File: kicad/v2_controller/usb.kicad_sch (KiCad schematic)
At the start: 23 parts, among them J1 USB_C_Receptacle_USB2.0, J2 USB_C_Receptacle_USB2.0, U4 NCP167BMX330TBG, U5 USBLC6-2P6, U6 USBLC6-2P6, U7 CP2102N-Axx-xQFN24

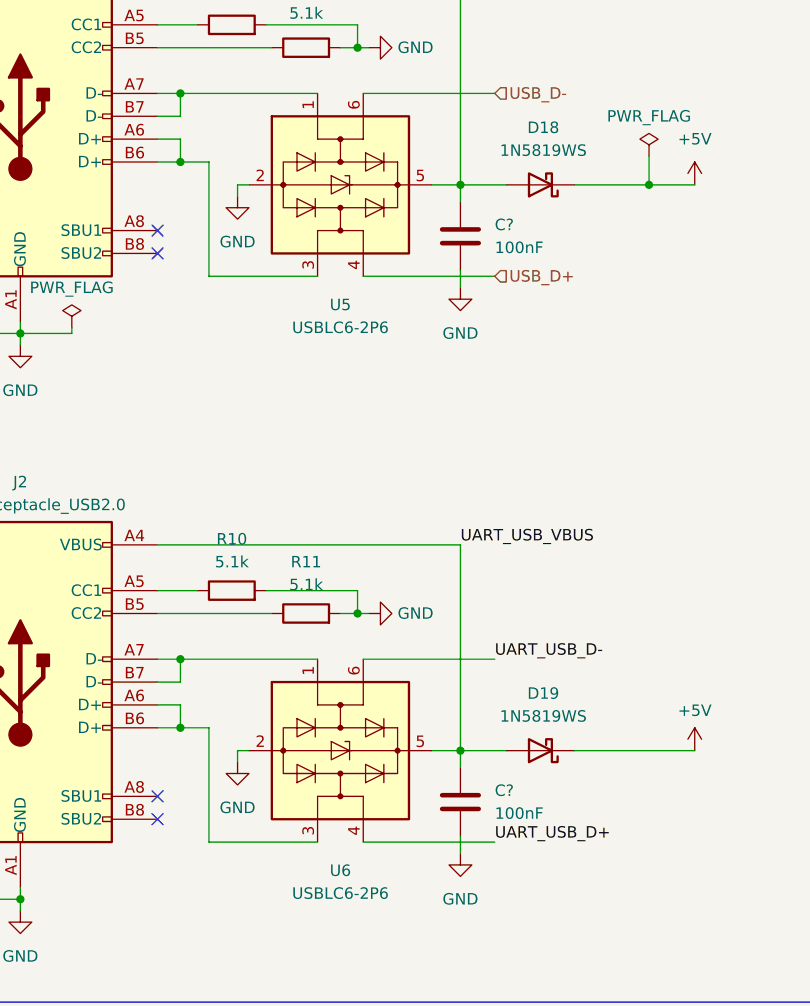
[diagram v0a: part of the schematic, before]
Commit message: [kicad] begin routing some traces
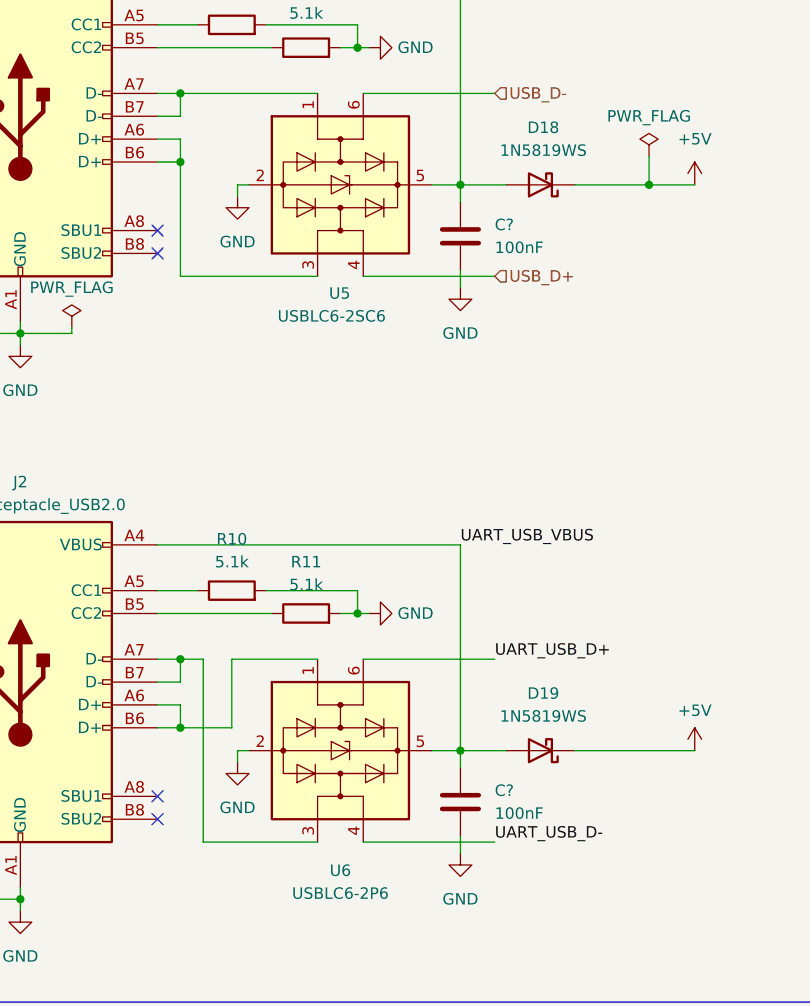
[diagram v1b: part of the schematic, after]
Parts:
- U5: value USBLC6-2P6 -> USBLC6-2SC6; footprint Package_TO_SOT_SMD:SOT-666 -> Package_TO_SOT_SMD:SOT-23-6; symbol Power_Protection:USBLC6-2P6 -> Power_Protection:USBLC6-2SC6; LCSC Part # C2827693 -> C2827654
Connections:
- net UART_USB_D+: now also U6.6 (I/O1); no longer U6.4 (I/O2)
- net UART_USB_D-: now also U6.4 (I/O2); no longer U6.6 (I/O1)
- net at J2.A7 (D-), J2.B7 (D-): now also U6.3 (I/O2); no longer U6.1 (I/O1)
- net at J2.A6 (D+), J2.B6 (D+): now also U6.1 (I/O1); no longer U6.3 (I/O2)
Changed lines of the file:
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@@
   (junction (at 175.895 69.215) (diameter 0) (color 0 0 0 0)
   )
+  (junction (at 63.5 54.61) (diameter 0) (color 0 0 0 0)
+  )
   (junction (at 213.36 42.545) (diameter 0) (color 0 0 0 0)
   )
+  (junction (at 63.5 109.855) (diameter 0) (color 0 0 0 0)
+  )
+  (junction (at 45.72 73.66) (diameter 0) (color 0 0 0 0)
+  )
+  (junction (at 213.36 34.925) (diameter 0) (color 0 0 0 0)
+  )
+  (junction (at 91.44 177.8) (diameter 0) (color 0 0 0 0)
+  )
+  (junction (at 91.44 175.26) (diameter 0) (color 0 0 0 0)
+  )
+  (junction (at 94.615 120.015) (diameter 0) (color 0 0 0 0)
+  )
+  (junction (at 45.72 136.525) (diameter 0) (color 0 0 0 0)
+  )
+  (junction (at 213.36 45.72) (diameter 0) (color 0 0 0 0)
+  )
+  (junction (at 95.25 167.64) (diameter 0) (color 0 0 0 0)
+  )
   (junction (at 63.5 46.99) (diameter 0) (color 0 0 0 0)
   )
-  (junction (at 45.72 73.66) (diameter 0) (color 0 0 0 0)
-  )
-  (junction (at 213.36 34.925) (diameter 0) (color 0 0 0 0)
-  )
-  (junction (at 91.44 177.8) (diameter 0) (color 0 0 0 0)
-  )
-  (junction (at 91.44 175.26) (diameter 0) (color 0 0 0 0)
-  )
-  (junction (at 94.615 120.015) (diameter 0) (color 0 0 0 0)
-  )
-  (junction (at 45.72 136.525) (diameter 0) (color 0 0 0 0)
-  )
-  (junction (at 213.36 45.72) (diameter 0) (color 0 0 0 0)
-  )
-  (junction (at 95.25 167.64) (diameter 0) (color 0 0 0 0)
-  )
   (junction (at 83.185 104.775) (diameter 0) (color 0 0 0 0)
   )
@@
   )
   (junction (at 50.8 167.64) (diameter 0) (color 0 0 0 0)
-  )
-  (junction (at 63.5 54.61) (diameter 0) (color 0 0 0 0)
-  )
-  (junction (at 63.5 109.855) (diameter 0) (color 0 0 0 0)
   )
   (junction (at 213.36 48.895) (diameter 0) (color 0 0 0 0)
@@
     (stroke (width 0) (type default))
   )
+  (wire (pts (xy 69.215 109.855) (xy 78.74 109.855))
+    (stroke (width 0) (type default))
+  )
   (wire (pts (xy 88.9 175.26) (xy 91.44 175.26))
     (stroke (width 0) (type default))
@@
     (stroke (width 0) (type default))
   )
-  (wire (pts (xy 66.675 117.475) (xy 66.675 130.175))
+  (wire (pts (xy 66.04 130.175) (xy 66.04 109.855))
     (stroke (width 0) (type default))
   )
@@
     (stroke (width 0) (type default))
   )
-  (wire (pts (xy 66.675 67.31) (xy 78.74 67.31))
+  (wire (pts (xy 63.5 46.99) (xy 78.74 46.99))
     (stroke (width 0) (type default))
   )
@@
     (stroke (width 0) (type default))
   )
+  (wire (pts (xy 63.5 54.61) (xy 63.5 67.31))
+    (stroke (width 0) (type default))
+  )
   (wire (pts (xy 60.96 46.99) (xy 63.5 46.99))
     (stroke (width 0) (type default))
@@
     (stroke (width 0) (type default))
   )
-  (wire (pts (xy 66.675 130.175) (xy 78.74 130.175))
+  (wire (pts (xy 78.74 130.175) (xy 66.04 130.175))
     (stroke (width 0) (type default))
   )
@@
     (stroke (width 0) (type default))
   )
+  (wire (pts (xy 78.74 67.31) (xy 63.5 67.31))
+    (stroke (width 0) (type default))
+  )
   (wire (pts (xy 83.82 67.31) (xy 98.425 67.31))
     (stroke (width 0) (type default))
@@
     (stroke (width 0) (type default))
   )
-  (wire (pts (xy 66.675 54.61) (xy 66.675 67.31))
-    (stroke (width 0) (type default))
-  )
   (wire (pts (xy 60.96 34.29) (xy 64.77 34.29))
     (stroke (width 0) (type default))
@@
     (stroke (width 0) (type default))
   )
-  (wire (pts (xy 63.5 109.855) (xy 78.74 109.855))
-    (stroke (width 0) (type default))
-  )
   (wire (pts (xy 107.315 120.015) (xy 120.65 120.015))
     (stroke (width 0) (type default))
@@
     (stroke (width 0) (type default))
   )
+  (wire (pts (xy 69.215 117.475) (xy 69.215 109.855))
+    (stroke (width 0) (type default))
+  )
+  (wire (pts (xy 66.04 109.855) (xy 63.5 109.855))
+    (stroke (width 0) (type default))
+  )
   (wire (pts (xy 94.615 120.015) (xy 94.615 121.92))
     (stroke (width 0) (type default))
@@
     (stroke (width 0) (type default))
   )
-  (wire (pts (xy 63.5 46.99) (xy 78.74 46.99))
-    (stroke (width 0) (type default))
-  )
   (wire (pts (xy 60.96 97.155) (xy 94.615 97.155))
     (stroke (width 0) (type default))
@@
     (stroke (width 0) (type default))
   )
-  (wire (pts (xy 63.5 117.475) (xy 66.675 117.475))
+  (wire (pts (xy 63.5 117.475) (xy 69.215 117.475))
     (stroke (width 0) (type default))
   )
@@
   )
   (wire (pts (xy 226.06 56.515) (xy 228.6 56.515))
-    (stroke (width 0) (type default))
-  )
-  (wire (pts (xy 63.5 54.61) (xy 66.675 54.61))
     (stroke (width 0) (type default))
   )
@@
     (effects (font (size 5 5) (thickness 1) bold (color 194 0 0 1)) (justify left bottom))
   )
-  (label "UART_USB_D-" (at 98.425 109.855 0) (fields_autoplaced)
+  (label "UART_USB_D+" (at 98.425 109.855 0) (fields_autoplaced)
     (effects (font (size 1.27 1.27)) (justify left bottom))
   )
@@
     (effects (font (size 1.27 1.27)) (justify left bottom))
   )
-  (label "UART_USB_D+" (at 98.425 130.175 0) (fields_autoplaced)
+  (label "UART_USB_D-" (at 98.425 130.175 0) (fields_autoplaced)
     (effects (font (size 1.27 1.27)) (justify left bottom))
   )
@@
     )
   )
-  (symbol (lib_id "Power_Protection:USBLC6-2P6") (at 81.28 57.15 270) (unit 1)
+  (symbol (lib_id "Power_Protection:USBLC6-2SC6") (at 81.28 57.15 270) (unit 1)
     (in_bom yes) (on_board yes) (dnp no)
-    (property "Reference" "U5" (at 81.28 70.485 90)
-      (effects (font (size 1.27 1.27)))
-    )
-    (property "Value" "USBLC6-2P6" (at 81.28 73.025 90)
-      (effects (font (size 1.27 1.27)))
-    )
-    (property "Footprint" "Package_TO_SOT_SMD:SOT-666" (at 68.58 57.15 0)
+    (property "Reference" "U5" (at 80.01 69.215 90)
+      (effects (font (size 1.27 1.27)) (justify left))
+    )
+    (property "Value" "USBLC6-2SC6" (at 74.295 71.755 90)
+      (effects (font (size 1.27 1.27)) (justify left))
+    )
+    (property "Footprint" "Package_TO_SOT_SMD:SOT-23-6" (at 68.58 57.15 0)
       (effects (font (size 1.27 1.27)) hide)
     )
@@
       (effects (font (size 1.27 1.27)) hide)
     )
-    (property "LCSC Part #" "C2827693" (at 81.28 57.15 0)
-      (effects (font (size 1.27 1.27)) hide)
-    )
+    (property "LCSC Part #" "C2827654" (at 81.28 57.15 0)
+      (effects (font (size 1.27 1.27)) hide)
+    )

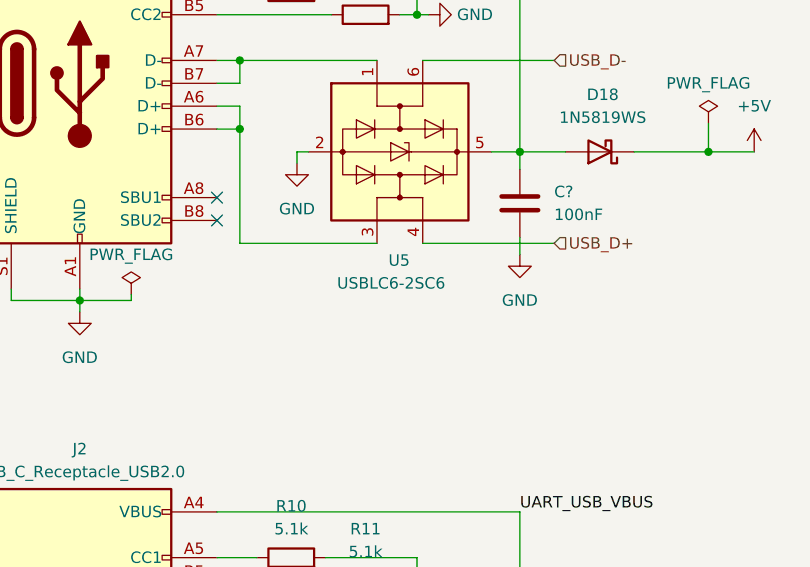
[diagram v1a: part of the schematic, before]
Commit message: [kicad] clean up additional PCB issues
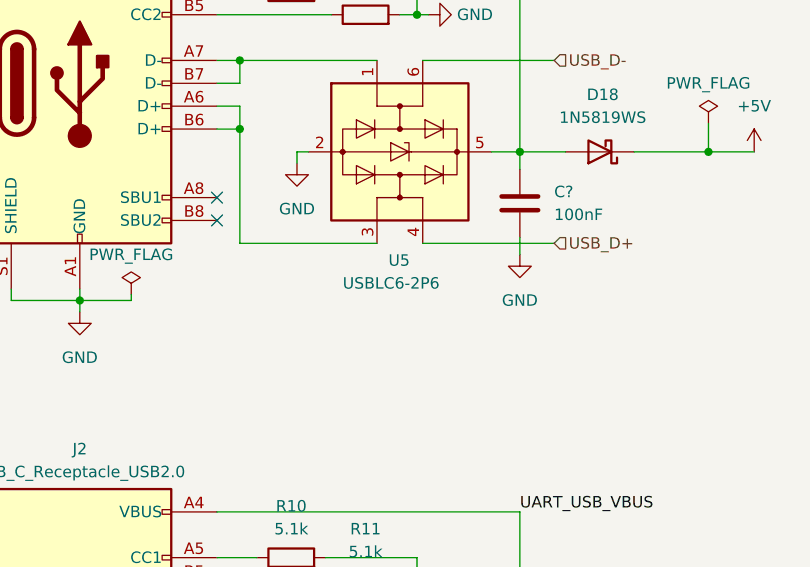
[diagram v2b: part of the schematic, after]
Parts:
- U5: value USBLC6-2SC6 -> USBLC6-2P6; footprint Package_TO_SOT_SMD:SOT-23-6 -> Package_TO_SOT_SMD:SOT-666; symbol Power_Protection:USBLC6-2SC6 -> Power_Protection:USBLC6-2P6; LCSC Part # C2827654 -> C2827693
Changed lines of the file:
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@@
     )
   )
-  (symbol (lib_id "Power_Protection:USBLC6-2SC6") (at 81.28 57.15 270) (unit 1)
+  (symbol (lib_id "Power_Protection:USBLC6-2P6") (at 81.28 57.15 270) (unit 1)
     (in_bom yes) (on_board yes) (dnp no)
     (property "Reference" "U5" (at 80.01 69.215 90)
       (effects (font (size 1.27 1.27)) (justify left))
     )
-    (property "Value" "USBLC6-2SC6" (at 74.295 71.755 90)
+    (property "Value" "USBLC6-2P6" (at 74.93 71.755 90)
       (effects (font (size 1.27 1.27)) (justify left))
     )
-    (property "Footprint" "Package_TO_SOT_SMD:SOT-23-6" (at 68.58 57.15 0)
+    (property "Footprint" "Package_TO_SOT_SMD:SOT-666" (at 68.58 57.15 0)
       (effects (font (size 1.27 1.27)) hide)
     )
@@
       (effects (font (size 1.27 1.27)) hide)
     )
-    (property "LCSC Part #" "C2827654" (at 81.28 57.15 0)
+    (property "LCSC Part #" "C2827693" (at 81.28 57.15 0)
       (effects (font (size 1.27 1.27)) hide)
     )

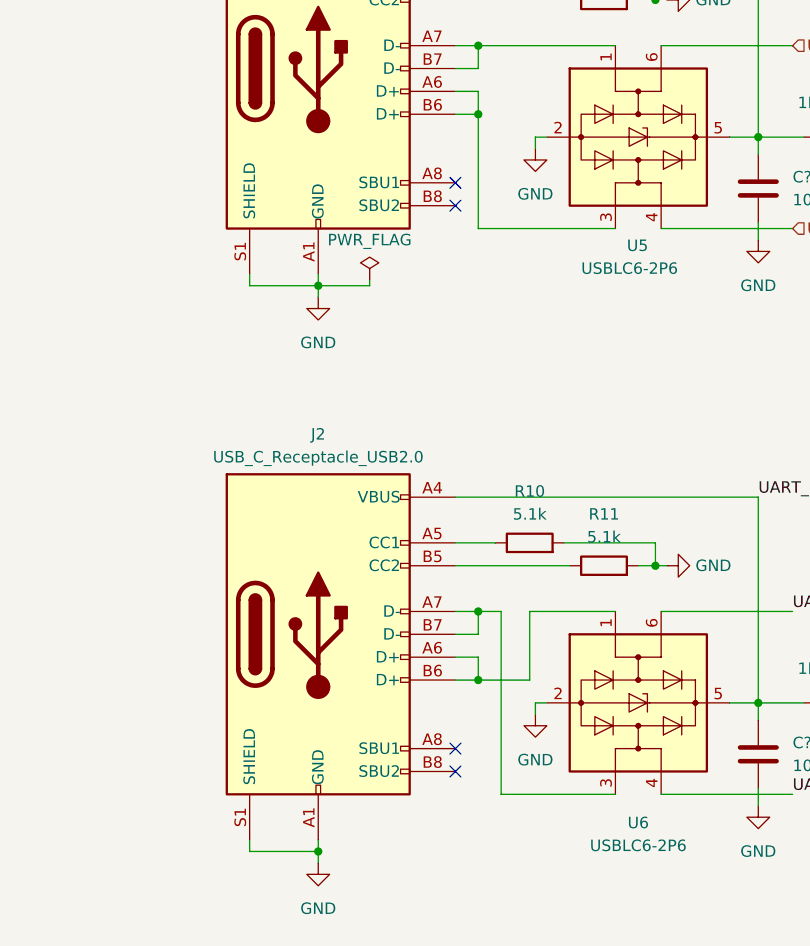
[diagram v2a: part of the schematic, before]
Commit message: [kicad] update USB connector symbols to have 14 pins
The USB connectors I am using have 14 pins rather than 16, so update
the symbol in the schematic to also have 14 pins.  This prevents Kicad
from complaining about these 2 extra pins when updating the PCB from the
schematic, even though they are not connected in the schematic.
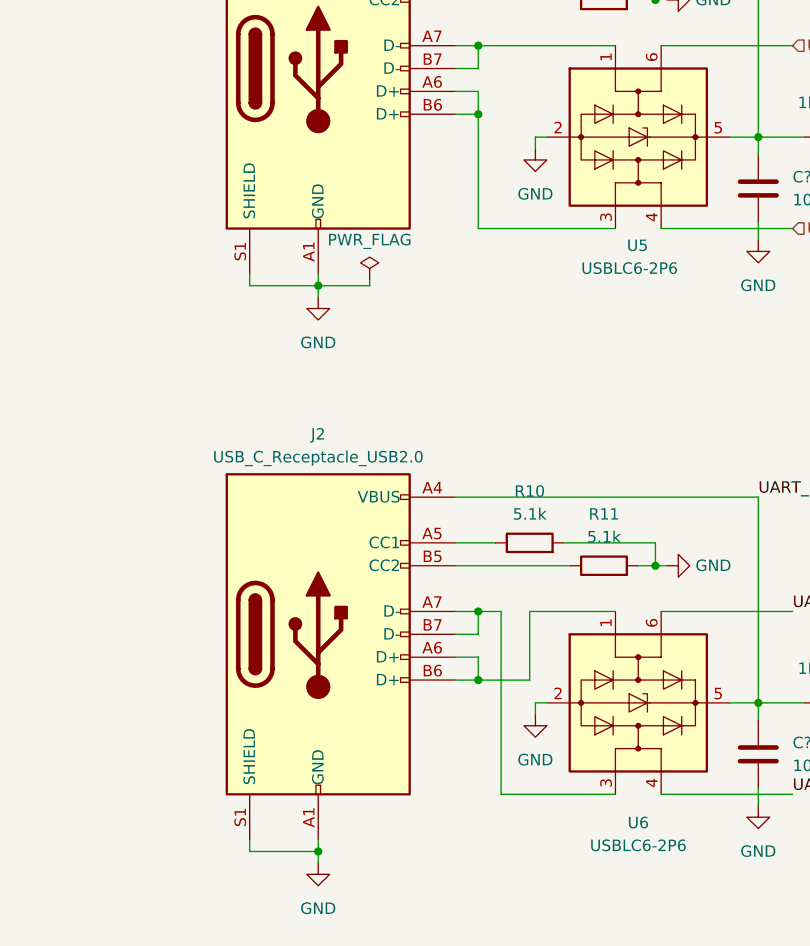
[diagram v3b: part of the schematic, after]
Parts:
- J1, J2: symbol Connector:USB_C_Receptacle_USB2.0 -> mantyl:USB_C_Receptacle_USB2.0_14Pin
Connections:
- no-connect marks 14 -> 10
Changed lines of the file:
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@@
   )
   (no_connect (at 226.06 64.135))
-  (no_connect (at 60.96 64.77))
-  (no_connect (at 60.96 127.635))
   (no_connect (at 226.06 94.615))
   (no_connect (at 226.06 74.295))
@@
   (no_connect (at 226.06 81.915))
   (no_connect (at 226.06 79.375))
-  (no_connect (at 60.96 62.23))
   (no_connect (at 226.06 71.755))
   (no_connect (at 226.06 86.995))
-  (no_connect (at 60.96 125.095))
   (wire (pts (xy 207.645 42.545) (xy 213.36 42.545))
     (stroke (width 0) (type default))
@@
     )
   )
-  (symbol (lib_name "USB_C_Receptacle_USB2.0_1") (lib_id "Connector:USB_C_Receptacle_USB2.0") (at 45.72 49.53 0) (unit 1)
+  (symbol (lib_id "mantyl:USB_C_Receptacle_USB2.0_14Pin") (at 45.72 49.53 0) (unit 1)
     (in_bom yes) (on_board yes) (dnp no) (fields_autoplaced)
     (property "Reference" "J1" (at 45.72 26.67 0)
@@
     (pin "A6")
     (pin "A7")
-    (pin "A8")
     (pin "A9")
     (pin "B1")
@@
     (pin "B6")
     (pin "B7")
-    (pin "B8")
     (pin "B9")
     (pin "S1")
@@
     )
   )
-  (symbol (lib_id "Connector:USB_C_Receptacle_USB2.0") (at 45.72 112.395 0) (unit 1)
+  (symbol (lib_id "mantyl:USB_C_Receptacle_USB2.0_14Pin") (at 45.72 112.395 0) (unit 1)
     (in_bom yes) (on_board yes) (dnp no) (fields_autoplaced)
     (property "Reference" "J2" (at 45.72 90.17 0)
@@
     (pin "A6")
     (pin "A7")
-    (pin "A8")
     (pin "A9")
     (pin "B1")
@@
     (pin "B6")
     (pin "B7")
-    (pin "B8")
     (pin "B9")
     (pin "S1")
